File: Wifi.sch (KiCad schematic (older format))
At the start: 6 parts

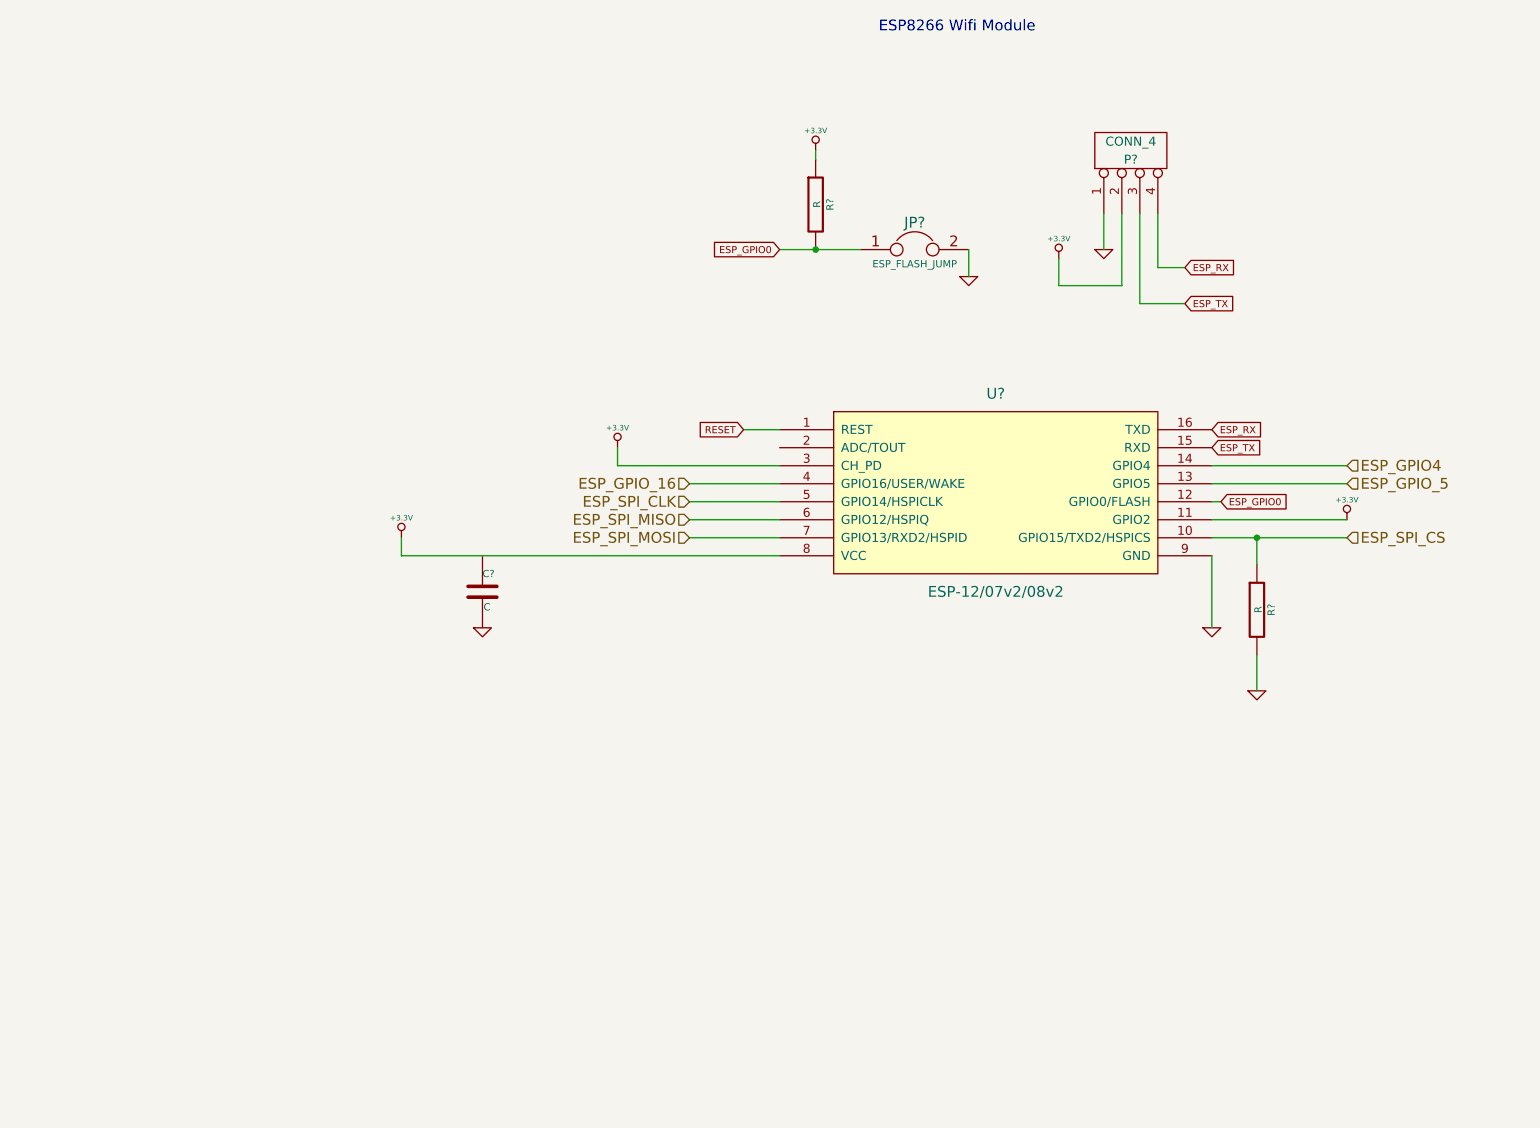
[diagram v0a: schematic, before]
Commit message: Add testpoints and tidy up
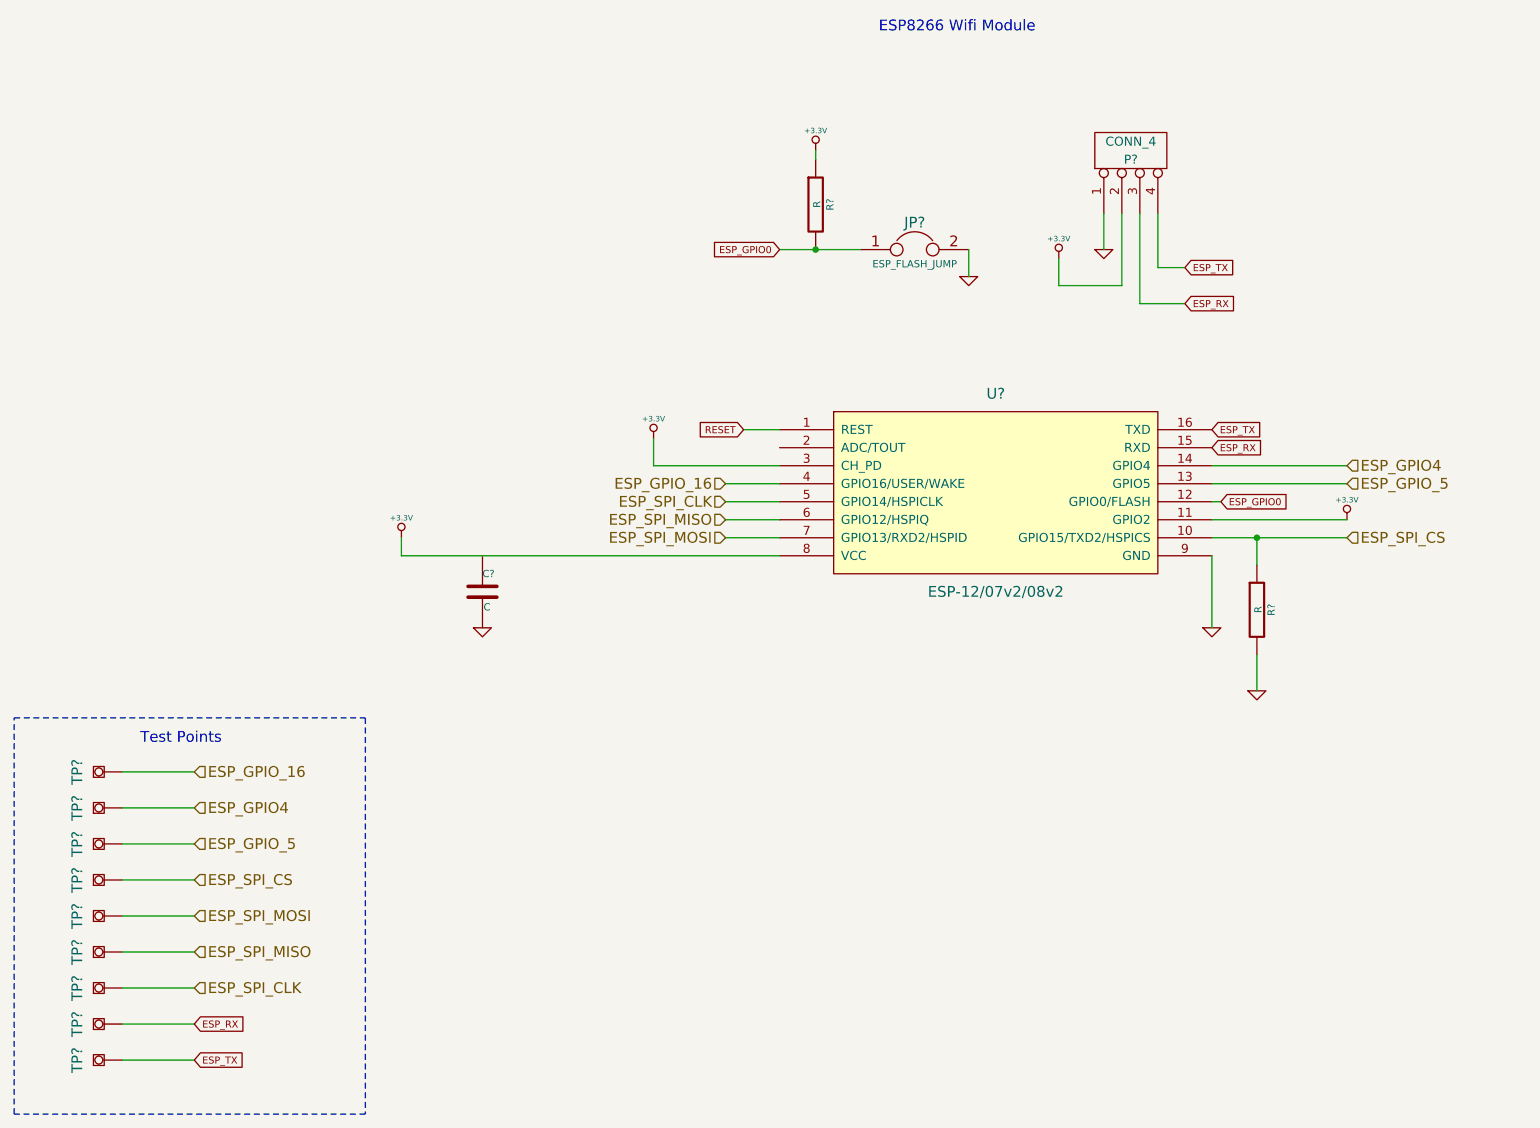
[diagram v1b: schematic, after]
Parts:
- added TP? (x9): TESTPOINT, symbol TESTPOINT
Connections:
- net ESP_GPIO4: now also TP?.1
- net ESP_GPIO_16: now also TP?.1
- net ESP_GPIO_5: now also TP?.1
- net ESP_RX: now also P?.3 (P3), U?.15 (RXD), TP?.1; no longer P?.4 (P4), U?.16 (TXD)
- net ESP_SPI_CLK: now also TP?.1
- net ESP_SPI_CS: now also TP?.1
- net ESP_SPI_MISO: now also TP?.1
- net ESP_SPI_MOSI: now also TP?.1
- net ESP_TX: now also P?.4 (P4), U?.16 (TXD), TP?.1; no longer P?.3 (P3), U?.15 (RXD)
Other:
- note added: "Test Points"
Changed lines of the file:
@@
 LIBS:ap1117e50g-13
 LIBS:irlml2246tr
+LIBS:testpoint
 LIBS:Wifi-GPIB-cache
 EELAYER 25 0
@@
 	1    0    0    -1
 $EndComp
-Wire Wire Line
-	6650 2700 6650 2900
 $Comp
 L +3.3V #PWR?
@@
 	1    0    0    -1
 $EndComp
-Wire Wire Line
-	6400 2950 6400 3100
-Wire Wire Line
-	6400 3100 6750 3100
-Wire Wire Line
-	6750 3100 6750 2700
-Wire Wire Line
-	6850 2700 6850 3200
-Wire Wire Line
-	6950 2700 6950 3000
-Wire Wire Line
-	6950 3000 7100 3000
-Wire Wire Line
-	6850 3200 7100 3200
+Text GLabel 7100 3200 2    39   Input ~ 0
+ESP_RX
 Text GLabel 7100 3000 2    39   Input ~ 0
-ESP_RX
-Text GLabel 7100 3200 2    39   Input ~ 0
 ESP_TX
 $Comp
@@
 	1    0    0    -1
 $EndComp
-Wire Wire Line
-	5050 2350 5050 2400
-Wire Wire Line
-	4850 2900 5300 2900
-Wire Wire Line
-	5900 2900 5900 3050
-Connection ~ 5050 2900
 Text GLabel 4850 2900 0    39   Input ~ 0
 ESP_GPIO0
 Text Notes 5400 1700 0    60   ~ 0
 ESP8266 Wifi Module
-Wire Wire Line
-	7250 4400 8000 4400
 $Comp
 L +3.3V #PWR?
@@
 L +3.3V #PWR?
 U 1 1 55667760
-P 3950 4000
-F 0 "#PWR?" H 3950 3960 30  0001 C CNN
-F 1 "+3.3V" H 3950 4110 30  0000 C CNN
-F 2 "" H 3950 4000 60  0000 C CNN
-F 3 "" H 3950 4000 60  0000 C CNN
-	1    3950 4000
-	1    0    0    -1
-$EndComp
-Wire Wire Line
-	3950 4100 4850 4100
-Wire Wire Line
-	4650 3900 4850 3900
+P 4150 3950
+F 0 "#PWR?" H 4150 3910 30  0001 C CNN
+F 1 "+3.3V" H 4150 4060 30  0000 C CNN
+F 2 "" H 4150 3950 60  0000 C CNN
+F 3 "" H 4150 3950 60  0000 C CNN
+	1    4150 3950
+	1    0    0    -1
+$EndComp
 Text GLabel 4650 3900 0    39   Input ~ 0
 RESET
-Wire Wire Line
-	3950 4000 3950 4100
-Wire Wire Line
-	7250 4300 7300 4300
-Wire Wire Line
-	7250 4500 8000 4500
-Wire Wire Line
-	7500 4500 7500 4650
 $Comp
 L GND #PWR?
@@
 	1    0    0    -1
 $EndComp
-Text GLabel 7250 3900 2    39   Input ~ 0
+Text GLabel 7250 4000 2    39   Input ~ 0
 ESP_RX
-Text GLabel 7250 4000 2    39   Input ~ 0
+Text GLabel 1600 7400 2    39   Input ~ 0
 ESP_TX
-Wire Wire Line
-	4850 4300 4350 4300
-Wire Wire Line
-	4850 4400 4350 4400
-Wire Wire Line
-	4850 4500 4350 4500
-Text HLabel 4350 4300 0    60   Input ~ 0
+Text HLabel 4550 4300 0    60   Input ~ 0
 ESP_SPI_CLK
-Text HLabel 4350 4400 0    60   Input ~ 0
+Text HLabel 4550 4400 0    60   Input ~ 0
 ESP_SPI_MISO
-Text HLabel 4350 4500 0    60   Input ~ 0
+Text HLabel 4550 4500 0    60   Input ~ 0
 ESP_SPI_MOSI
 $Comp
@@
 	1    0    0    -1
 $EndComp
-Wire Wire Line
-	7500 5350 7500 5150
-Connection ~ 7500 4500
 Text HLabel 8000 4500 2    60   Input ~ 0
 ESP_SPI_CS
-Wire Wire Line
-	4850 4600 2750 4600
-Wire Wire Line
-	2750 4600 2750 4500
 $Comp
 L +3.3V #PWR?
@@
 	1    0    0    -1
 $EndComp
-Wire Wire Line
-	7250 4600 7250 5000
 $Comp
 L GND #PWR?
@@
 	1    0    0    -1
 $EndComp
-Wire Wire Line
-	7250 4100 8000 4100
-Wire Wire Line
-	7250 4200 8000 4200
 Text GLabel 7300 4300 2    39   Input ~ 0
 ESP_GPIO0
@@
 Text HLabel 8000 4200 2    60   Input ~ 0
 ESP_GPIO_5
-Text HLabel 4350 4200 0    60   Input ~ 0
+Text HLabel 4550 4200 0    60   Input ~ 0
 ESP_GPIO_16
-Wire Wire Line
-	4850 4200 4350 4200
+$Comp
+L TESTPOINT TP?
+U 1 1 55669763
+P 1200 5800
+F 0 "TP?" H 1200 6050 60  0000 C CNN
+F 1 "TESTPOINT" H 1200 5750 60  0001 C CNN
+F 2 "" H 1200 5800 60  0000 C CNN
+F 3 "" H 1200 5800 60  0000 C CNN
+	1    1200 5800
+	0    -1   -1   0
+$EndComp
+Wire Wire Line
+	6650 2700 6650 2900
+Wire Wire Line
+	6400 2950 6400 3100
+Wire Wire Line
+	6400 3100 6750 3100
+Wire Wire Line
+	6750 3100 6750 2700
+Wire Wire Line
+	6850 2700 6850 3200
+Wire Wire Line
+	6950 2700 6950 3000
+Wire Wire Line
+	6950 3000 7100 3000
+Wire Wire Line
+	6850 3200 7100 3200
+Wire Wire Line
+	5050 2350 5050 2400
+Wire Wire Line
+	4850 2900 5300 2900
+Wire Wire Line
+	5900 2900 5900 3050
+Connection ~ 5050 2900
+Wire Wire Line
+	7250 4400 8000 4400
+Wire Wire Line
+	4150 4100 4850 4100
+Wire Wire Line
+	4650 3900 4850 3900
+Wire Wire Line
+	4150 3950 4150 4100
+Wire Wire Line
+	7250 4300 7300 4300
+Wire Wire Line
+	7250 4500 8000 4500
+Wire Wire Line
+	7500 4500 7500 4650
+Wire Wire Line
+	7500 5350 7500 5150
+Connection ~ 7500 4500
+Wire Wire Line
+	4850 4600 2750 4600
+Wire Wire Line
+	2750 4600 2750 4500
+Wire Wire Line
+	7250 4600 7250 5000
+Wire Wire Line
+	7250 4100 8000 4100
+Wire Wire Line
+	7250 4200 8000 4200
+Wire Wire Line
+	4850 4200 4550 4200
+Wire Wire Line
+	4850 4300 4550 4300
+Wire Wire Line
+	4850 4400 4550 4400
+Wire Wire Line
+	4850 4500 4550 4500
+$Comp
+L TESTPOINT TP?
+U 1 1 55669E4F
+P 1200 6000
+F 0 "TP?" H 1200 6250 60  0000 C CNN
+F 1 "TESTPOINT" H 1200 5950 60  0001 C CNN
+F 2 "" H 1200 6000 60  0000 C CNN
+F 3 "" H 1200 6000 60  0000 C CNN
+	1    1200 6000
+	0    -1   -1   0
+$EndComp
+$Comp
+L TESTPOINT TP?
+U 1 1 55669E83
+P 1200 6200
+F 0 "TP?" H 1200 6450 60  0000 C CNN
+F 1 "TESTPOINT" H 1200 6150 60  0001 C CNN
+F 2 "" H 1200 6200 60  0000 C CNN
+F 3 "" H 1200 6200 60  0000 C CNN
+	1    1200 6200
+	0    -1   -1   0
+$EndComp
+$Comp
+L TESTPOINT TP?
+U 1 1 55669EAD
+P 1200 6400
+F 0 "TP?" H 1200 6650 60  0000 C CNN
+F 1 "TESTPOINT" H 1200 6350 60  0001 C CNN
+F 2 "" H 1200 6400 60  0000 C CNN
+F 3 "" H 1200 6400 60  0000 C CNN
+	1    1200 6400
+	0    -1   -1   0
+$EndComp
+$Comp
+L TESTPOINT TP?
+U 1 1 55669F01
+P 1200 6600
+F 0 "TP?" H 1200 6850 60  0000 C CNN
+F 1 "TESTPOINT" H 1200 6550 60  0001 C CNN
+F 2 "" H 1200 6600 60  0000 C CNN
+F 3 "" H 1200 6600 60  0000 C CNN
+	1    1200 6600
+	0    -1   -1   0
+$EndComp
+$Comp
+L TESTPOINT TP?
+U 1 1 55669F33
+P 1200 6800
+F 0 "TP?" H 1200 7050 60  0000 C CNN
+F 1 "TESTPOINT" H 1200 6750 60  0001 C CNN
+F 2 "" H 1200 6800 60  0000 C CNN
+F 3 "" H 1200 6800 60  0000 C CNN
+	1    1200 6800
+	0    -1   -1   0
+$EndComp
+$Comp
+L TESTPOINT TP?
+U 1 1 55669F6B
+P 1200 7000
+F 0 "TP?" H 1200 7250 60  0000 C CNN
+F 1 "TESTPOINT" H 1200 6950 60  0001 C CNN
+F 2 "" H 1200 7000 60  0000 C CNN
+F 3 "" H 1200 7000 60  0000 C CNN
+	1    1200 7000
+	0    -1   -1   0
+$EndComp
+Wire Wire Line
+	1200 5800 1600 5800
+Wire Wire Line
+	1200 6000 1600 6000
+Wire Wire Line
+	1200 6200 1600 6200
+Wire Wire Line
+	1200 6400 1600 6400
+Wire Wire Line
+	1200 6600 1600 6600
+Wire Wire Line
+	1200 6800 1600 6800
+Wire Wire Line
+	1200 7000 1600 7000
+Text HLabel 1600 5800 2    60   Input ~ 0
+ESP_GPIO_16
+Text HLabel 1600 7000 2    60   Input ~ 0
+ESP_SPI_CLK
+Text HLabel 1600 6800 2    60   Input ~ 0
+ESP_SPI_MISO
+Text HLabel 1600 6600 2    60   Input ~ 0
+ESP_SPI_MOSI
+Text HLabel 1600 6400 2    60   Input ~ 0
+ESP_SPI_CS
+Text HLabel 1600 6200 2    60   Input ~ 0
+ESP_GPIO_5
+Text HLabel 1600 6000 2    60   Input ~ 0
+ESP_GPIO4
+$Comp
+L TESTPOINT TP?
+U 1 1 5566A6E7
+P 1200 7200
+F 0 "TP?" H 1200 7450 60  0000 C CNN
+F 1 "TESTPOINT" H 1200 7150 60  0001 C CNN
+F 2 "" H 1200 7200 60  0000 C CNN
+F 3 "" H 1200 7200 60  0000 C CNN
+	1    1200 7200
+	0    -1   -1   0
+$EndComp
+Wire Wire Line
+	1200 7200 1600 7200
+$Comp
+L TESTPOINT TP?
+U 1 1 5566A71B
+P 1200 7400
+F 0 "TP?" H 1200 7650 60  0000 C CNN
+F 1 "TESTPOINT" H 1200 7350 60  0001 C CNN
+F 2 "" H 1200 7400 60  0000 C CNN
+F 3 "" H 1200 7400 60  0000 C CNN
+	1    1200 7400
+	0    -1   -1   0
+$EndComp
+Wire Wire Line
+	1200 7400 1600 7400
+Text GLabel 1600 7200 2    39   Input ~ 0
+ESP_RX
+Text GLabel 7250 3900 2    39   Input ~ 0
+ESP_TX
+Wire Notes Line
+	600  5500 2550 5500
+Wire Notes Line
+	2550 5500 2550 7700
+Wire Notes Line
+	2550 7700 600  7700
+Wire Notes Line
+	600  7700 600  5500
+Text Notes 1300 5650 0    60   ~ 0
+Test Points
 $EndSCHEMATC

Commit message: ESP Serial interface
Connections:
- net ESP_SPI_CS: no longer R?.1, U?.10 (GPIO15/TXD2/HSPICS)
- net ESP_SPI_MOSI: no longer U?.7 (GPIO13/RXD2/HSPID)
- net RESET renamed ESP_RESET
- new net ESP_SPI_CS/TXD2: R?.1, U?.10 (GPIO15/TXD2/HSPICS)
- new net ESP_SPI_MOSI/RXD2: U?.7 (GPIO13/RXD2/HSPID)
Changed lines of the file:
@@
 	1    0    0    -1
 $EndComp
-Text GLabel 4650 3900 0    39   Input ~ 0
-RESET
 $Comp
 L GND #PWR?
@@
 ESP_SPI_MISO
 Text HLabel 4550 4500 0    60   Input ~ 0
-ESP_SPI_MOSI
+ESP_SPI_MOSI/RXD2
 $Comp
 L R R?
@@
 $EndComp
 Text HLabel 8000 4500 2    60   Input ~ 0
-ESP_SPI_CS
+ESP_SPI_CS/TXD2
 $Comp
 L +3.3V #PWR?
@@
 Text Notes 1300 5650 0    60   ~ 0
 Test Points
+Text HLabel 4650 3900 0    39   Input ~ 0
+ESP_RESET
 $EndSCHEMATC
